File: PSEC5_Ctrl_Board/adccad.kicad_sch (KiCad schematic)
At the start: 0 parts

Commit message: Ports are Finished, wiring and finalization needed
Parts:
- added U13, U14: LTC2600CGN_PBF, LTC2600CGN_PBF:SSOP-16_GN, symbol PSEC5_ctrlbd:LTC2600CGN_PBF
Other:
- note added: "DAC"
- note added: "DAC 1"
- note added: "DAC 2"
- note added: "From FPGA"
- note added: "To Samtec"

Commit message: Large Updates, Touching up before further aproval
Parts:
- added C23: 0.1u, symbol Device:C
- added C35, C45, C80: 0.1u, Capacitor_SMD:C_0201_0603Metric, symbol Device:C_Small
- added R17: 7.5k, symbol Device:R_US
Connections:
- net GND: now reaches U14.1 (GND)
- net GND: now also U13.1 (GND), U13.10 (SDO), C23.2, C35.2, C45.2, C80.2
- net DAC2_VCC_5V0: now reaches U14.16 (VCC)
- net DAC2_VCC_5V0: now also U13.16 (VCC), C35.1, C45.1, R17.2
- net DISCBIAS: now reaches U14.2 (VOUTA)
- net WBUFBIAS: now reaches U14.3 (VOUTB)
- net READBIAS1: now reaches U14.4 (VOUTC)
- net READBIAS2: now reaches U14.5 (VOUTD)
- net DAC_VRef: now reaches U14.6 (REF)
- net DAC_VRef: now also U13.6 (REF), C23.1, C80.1
- net at U13.11 (*CLR): now also R17.1
- net THRES5: now reaches U13.12 (VOUTE)
- net THRES6: now reaches U13.13 (VOUTF)
- net THRES7: now reaches U13.14 (VOUTG)
- net THRES8: now reaches U13.15 (VOUTH)
- net THRES1: now reaches U13.2 (VOUTA)
- net THRES2: now reaches U13.3 (VOUTB)
- net THRES3: now reaches U13.4 (VOUTC)
- net THRES4: now reaches U13.5 (VOUTD)
- net DAC2_CS/LD: now reaches U13.7 (*CS/LD)
- net DAC2_SCK: now reaches U13.8 (SCK)
- net DAC2_SDI: now reaches U13.9 (SDI)
- no-connect marks 0 -> 4
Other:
- moved on the sheet: U13, U14

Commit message: minor changes
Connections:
- net THRES1 renamed Disc_Thresh1
- net THRES2 renamed Disc_Thresh2
- net THRES3 renamed Disc_Thresh3
- net THRES4 renamed Disc_Thresh4
- net THRES5 renamed Disc_Thresh5
- net THRES6 renamed Disc_Thresh6
- net THRES7 renamed Disc_Thresh7
- net THRES8 renamed Disc_Thresh8
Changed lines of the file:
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@@
 		)
 	)
-	(global_label "THRES1"
+	(global_label "Disc_Thresh1"
 		(shape output)
 		(at 74.93 54.61 0)
@@
 		)
 		(property "Intersheetrefs" "${INTERSHEET_REFS}"
-			(at 85.0513 54.61 0)
-			(effects
-				(font
-					(size 1.27 1.27)
-				)
-				(justify left)
-				(hide yes)
-			)
-		)
-	)
-	(global_label "THRES4"
+			(at 90.2523 54.61 0)
+			(effects
+				(font
+					(size 1.27 1.27)
+				)
+				(justify left)
+				(hide yes)
+			)
+		)
+	)
+	(global_label "Disc_Thresh4"
 		(shape output)
 		(at 74.93 62.23 0)
@@
 		)
 		(property "Intersheetrefs" "${INTERSHEET_REFS}"
-			(at 85.0513 62.23 0)
+			(at 90.2523 62.23 0)
 			(effects
 				(font
@@
 		)
 	)
-	(global_label "THRES8"
+	(global_label "Disc_Thresh8"
 		(shape output)
 		(at 74.93 72.39 0)
@@
 		)
 		(property "Intersheetrefs" "${INTERSHEET_REFS}"
-			(at 85.0513 72.39 0)
-			(effects
-				(font
-					(size 1.27 1.27)
-				)
-				(justify left)
-				(hide yes)
-			)
-		)
-	)
-	(global_label "THRES2"
+			(at 90.2523 72.39 0)
+			(effects
+				(font
+					(size 1.27 1.27)
+				)
+				(justify left)
+				(hide yes)
+			)
+		)
+	)
+	(global_label "Disc_Thresh2"
 		(shape output)
 		(at 74.93 57.15 0)
@@
 		)
 		(property "Intersheetrefs" "${INTERSHEET_REFS}"
-			(at 85.0513 57.15 0)
-			(effects
-				(font
-					(size 1.27 1.27)
-				)
-				(justify left)
-				(hide yes)
-			)
-		)
-	)
-	(global_label "THRES7"
+			(at 90.2523 57.15 0)
+			(effects
+				(font
+					(size 1.27 1.27)
+				)
+				(justify left)
+				(hide yes)
+			)
+		)
+	)
+	(global_label "Disc_Thresh7"
 		(shape output)
 		(at 74.93 69.85 0)
@@
 		)
 		(property "Intersheetrefs" "${INTERSHEET_REFS}"
-			(at 85.0513 69.85 0)
-			(effects
-				(font
-					(size 1.27 1.27)
-				)
-				(justify left)
-				(hide yes)
-			)
-		)
-	)
-	(global_label "THRES6"
+			(at 90.2523 69.85 0)
+			(effects
+				(font
+					(size 1.27 1.27)
+				)
+				(justify left)
+				(hide yes)
+			)
+		)
+	)
+	(global_label "Disc_Thresh6"
 		(shape output)
 		(at 74.93 67.31 0)
@@
 		)
 		(property "Intersheetrefs" "${INTERSHEET_REFS}"
-			(at 85.0513 67.31 0)
-			(effects
-				(font
-					(size 1.27 1.27)
-				)
-				(justify left)
-				(hide yes)
-			)
-		)
-	)
-	(global_label "THRES5"
+			(at 90.2523 67.31 0)
+			(effects
+				(font
+					(size 1.27 1.27)
+				)
+				(justify left)
+				(hide yes)
+			)
+		)
+	)
+	(global_label "Disc_Thresh5"
 		(shape output)
 		(at 74.93 64.77 0)
@@
 		)
 		(property "Intersheetrefs" "${INTERSHEET_REFS}"
-			(at 85.0513 64.77 0)
+			(at 90.2523 64.77 0)
 			(effects
 				(font
@@
 		)
 	)
-	(global_label "THRES3"
+	(global_label "Disc_Thresh3"
 		(shape output)
 		(at 74.93 59.69 0)
@@
 		)
 		(property "Intersheetrefs" "${INTERSHEET_REFS}"
-			(at 85.0513 59.69 0)
-			(effects
-				(font
+			(at 90.2523 59.69 0)
+			(effects
+				(font

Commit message: Schematic is "done" ;( (999+ ERC errors)
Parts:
- added R56: 7.5k, Capacitor_SMD:C_0603_1608Metric, symbol Device:R_US
- C90: renamed from C23; footprint (none) -> Capacitor_SMD:C_0603_1608Metric
- R77: renamed from R17; footprint (none) -> Capacitor_SMD:C_0603_1608Metric
- renumbered C35 to C92
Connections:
- net DAC2_CS/LD is gone; now on net CS/LD_DAC*: U13.7 (*CS/LD)
- net DAC2_SCK is gone; now on net SCK_DAC: U13.8 (SCK)
- net GND: now also U14.10 (SDO)
- net at U14.11 (*CLR): now also R56.1
- net CS/LD_DAC*: now reaches U14.7 (*CS/LD)
- net SCK_DAC: now reaches U14.8 (SCK)
- net SDI_DAC_BIAS: now reaches U14.9 (SDI)
- net DAC2_SDI renamed SDI_DAC_THRES
- net DAC2_VCC_5V0 renamed 3V3_DUT
- net 3V3_DUT: no longer R77.2
- net DAC_VRef renamed 1V8_DUT
- new net CLR_DAC*: R56.2, R77.2
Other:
- note added: "Currently, both DAC's have the following pins shorted:* *CS/LD* SCK *CLR However, the SDI pins are independent of eachother"
- note added: "From Kria"
- note added: "NOTE: DAC will run at 3V3"
- note added: "To DUT"
- note removed: "DAC"
- note removed: "DAC 1"
- note removed: "DAC 2"
- note removed: "From FPGA"
- note removed: "To Samtec"

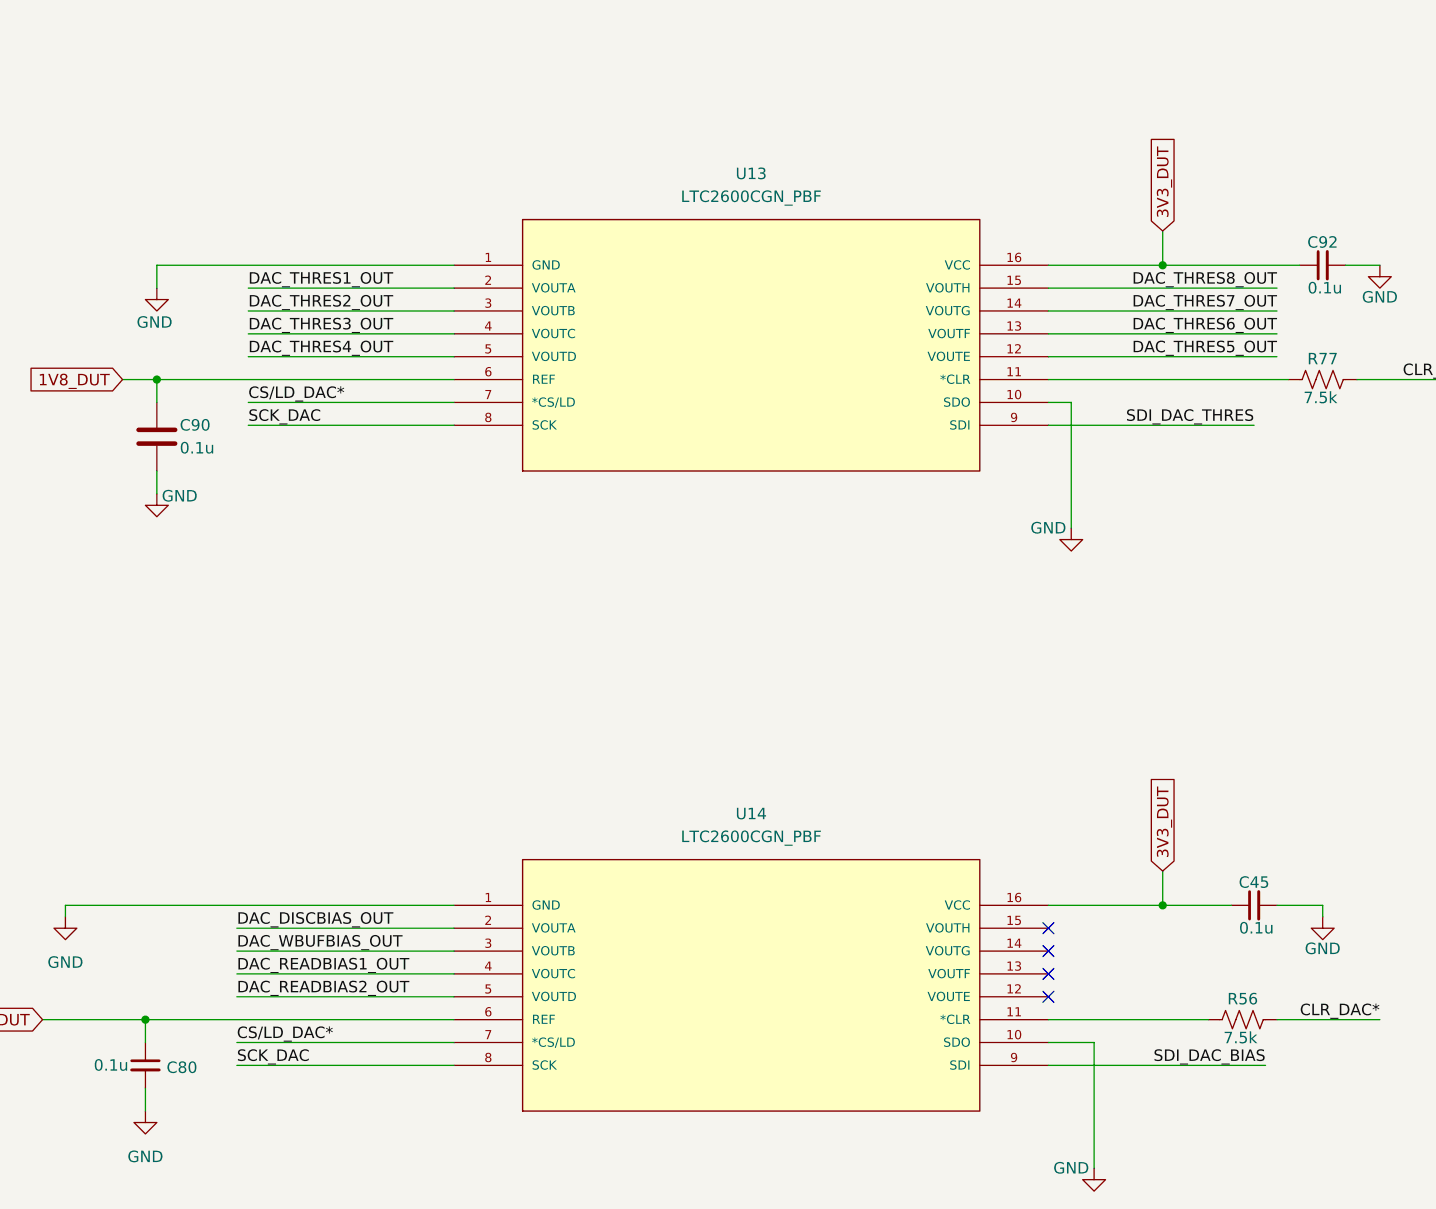
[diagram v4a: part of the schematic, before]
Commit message: Deleted some Pages, still lots of errors :(
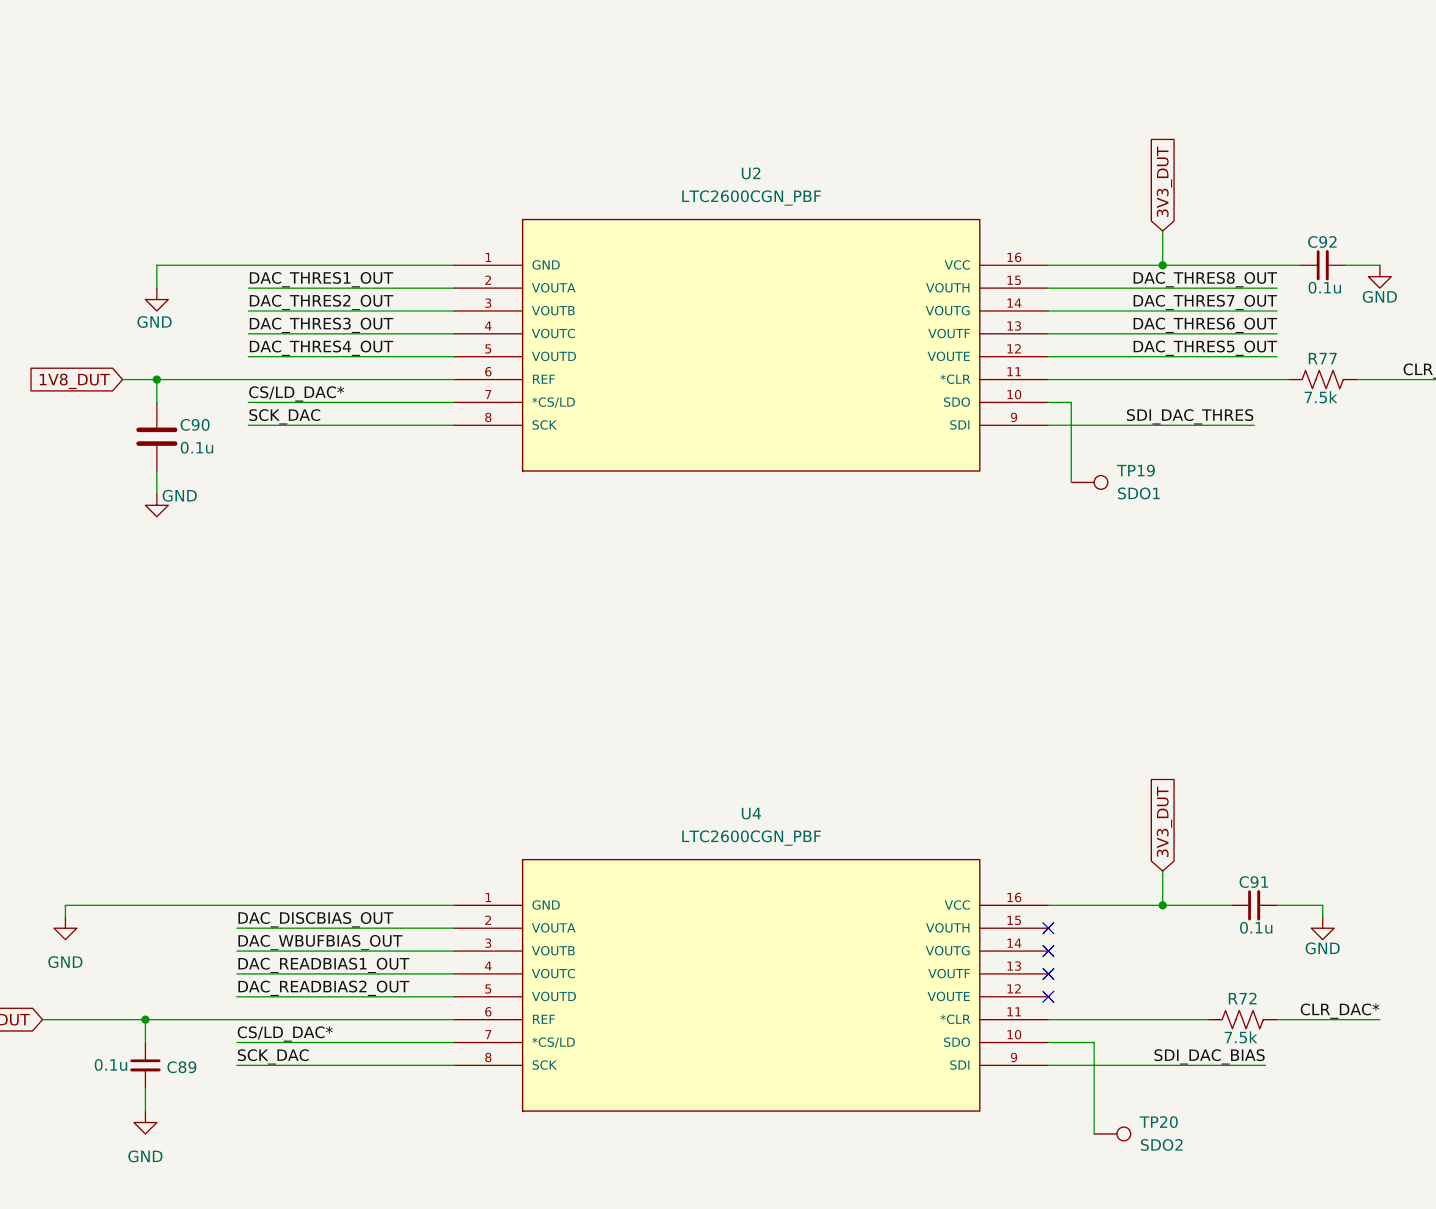
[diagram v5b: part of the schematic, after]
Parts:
- added TP19: SDO1, symbol Connector:TestPoint
- added TP20: SDO2, symbol Connector:TestPoint
- renumbered C80 to C89, C45 to C91, R56 to R72, U13 to U2, U14 to U4
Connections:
- net GND: no longer U2.10 (SDO), U4.10 (SDO)
- new net: TP19.1, U2.10 (SDO)
- new net: TP20.1, U4.10 (SDO)
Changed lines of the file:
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@@
-	(wire
-		(pts
-			(xy 218.44 91.44) (xy 218.44 77.47)
-		)
-		(stroke
-			(width 0)
-			(type default)
-		)
-	)
 	(wire
 		(pts
@@
 	(wire
 		(pts
-			(xy 220.98 148.59) (xy 220.98 162.56)
-		)
-		(stroke
-			(width 0)
-			(type default)
-		)
-	)
-	(wire
-		(pts
 			(xy 116.84 64.77) (xy 116.84 62.23)
 		)
@@
 	(wire
 		(pts
+			(xy 220.98 148.59) (xy 220.98 158.75)
+		)
+		(stroke
+			(width 0)
+			(type default)
+		)
+	)
+	(wire
+		(pts
 			(xy 218.44 77.47) (xy 215.9 77.47)
 		)
@@
 		(pts
 			(xy 250.19 74.93) (xy 264.16 74.93)
+		)
+		(stroke
+			(width 0)
+			(type default)
+		)
+	)
+	(wire
+		(pts
+			(xy 218.44 77.47) (xy 218.44 86.36)
 		)
 		(stroke
@@
 			)
 			(justify right)
+		)
+	)
+	(symbol
+		(lib_id "Connector:TestPoint")
+		(at 218.44 86.36 270)
+		(unit 1)
+		(exclude_from_sim no)
+		(in_bom yes)
+		(on_board yes)
+		(dnp no)
+		(fields_autoplaced yes)
+		(property "Reference" "TP19"
+			(at 223.52 85.0899 90)
+			(effects
+				(font
+					(size 1.27 1.27)
+				)
+				(justify left)
+			)
+		)
+		(property "Value" "SDO1"
+			(at 223.52 87.6299 90)
+			(effects
+				(font
+					(size 1.27 1.27)
+				)
+				(justify left)
+			)
+		)
+		(property "Footprint" ""
+			(at 218.44 91.44 0)
+			(effects
+				(font
+					(size 1.27 1.27)
+				)
+				(hide yes)
+			)
+		)
+		(property "Datasheet" "~"
+			(at 218.44 91.44 0)
+			(effects
+				(font
+					(size 1.27 1.27)
+				)
+				(hide yes)
+			)
+		)
+		(property "Description" "test point"
+			(at 218.44 86.36 0)
+			(effects
+				(font
+					(size 1.27 1.27)
+				)
+				(hide yes)
+			)
+		)
+		(pin "1"
+		)
+		(instances
+			(project ""
+				(path "/165f2ae6-d522-4adf-a6c4-bb137b209d33/1f6d7a03-cfad-4370-8d2b-49ab19e248d8/9bd9ffce-acff-4ff9-8380-cb9ceb30e6db"
+					(reference "TP19")
+					(unit 1)
+				)
+			)
 		)
 	)
@@
 		(on_board yes)
 		(dnp no)
-		(property "Reference" "#PWR053"
+		(property "Reference" "#PWR0113"
 			(at 116.84 93.98 0)
 			(effects
@@
 		(instances
 			(project "PSEC5_Ctrl_Board"
-				(path "/165f2ae6-d522-4adf-a6c4-bb137b209d33/7f8209d2-4c0c-4014-a327-54471b9e4269"
-					(reference "#PWR053")
-					(unit 1)
-				)
 				(path "/165f2ae6-d522-4adf-a6c4-bb137b209d33/1f6d7a03-cfad-4370-8d2b-49ab19e248d8/9bd9ffce-acff-4ff9-8380-cb9ceb30e6db"
 					(reference "#PWR0113")
@@
 	(symbol
 		(lib_id "power:GND")
-		(at 220.98 162.56 0)
-		(unit 1)
-		(exclude_from_sim no)
-		(in_bom yes)
-		(on_board yes)
-		(dnp no)
-		(property "Reference" "#PWR044"
-			(at 220.98 168.91 0)
-			(effects
-				(font
-					(size 1.27 1.27)
-				)
-				(hide yes)
-			)
-		)
-		(property "Value" "GND"
-			(at 218.44 162.56 0)
-			(effects
-				(font
-					(size 1.27 1.27)
-				)
-			)
-		)
-		(property "Footprint" ""
-			(at 220.98 162.56 0)
-			(effects
-				(font
-					(size 1.27 1.27)
-				)
-				(hide yes)
-			)
-		)
-		(property "Datasheet" ""
-			(at 220.98 162.56 0)
-			(effects
-				(font
-					(size 1.27 1.27)
-				)
-				(hide yes)
-			)
-		)
-		(property "Description" "Power symbol creates a global label with name \"GND\" , ground"
-			(at 220.98 162.56 0)
-			(effects
-				(font
-					(size 1.27 1.27)
-				)
-				(hide yes)
-			)
-		)
-		(pin "1"
-		)
-		(instances
-			(project "PSEC5_Ctrl_Board"
-				(path "/165f2ae6-d522-4adf-a6c4-bb137b209d33/7f8209d2-4c0c-4014-a327-54471b9e4269"
-					(reference "#PWR044")
-					(unit 1)
-				)
-				(path "/165f2ae6-d522-4adf-a6c4-bb137b209d33/1f6d7a03-cfad-4370-8d2b-49ab19e248d8/9bd9ffce-acff-4ff9-8380-cb9ceb30e6db"
-					(reference "#PWR0115")
-					(unit 1)
-				)
-			)
-		)
-	)
-	(symbol
-		(lib_id "power:GND")
 		(at 106.68 134.62 0)
 		(unit 1)
@@
 		(dnp no)
 		(fields_autoplaced yes)
-		(property "Reference" "U14"
+		(property "Reference" "U4"
 			(at 182.88 123.19 0)
 			(effects
@@
 		)
 		(pin "5"
-		)
-		(instances
-			(project "PSEC5_Ctrl_Board"
-				(path "/165f2ae6-d522-4adf-a6c4-bb137b209d33/7f8209d2-4c0c-4014-a327-54471b9e4269"
-					(reference "U14")
-					(unit 1)
-				)
-				(path "/165f2ae6-d522-4adf-a6c4-bb137b209d33/1f6d7a03-cfad-4370-8d2b-49ab19e248d8/9bd9ffce-acff-4ff9-8380-cb9ceb30e6db"
-					(reference "U4")
-					(unit 1)
-				)
-			)
-		)
-	)
-	(symbol
-		(lib_id "power:GND")
-		(at 218.44 91.44 0)
-		(unit 1)
-		(exclude_from_sim no)
-		(in_bom yes)
-		(on_board yes)
-		(dnp no)
-		(property "Reference" "#PWR0114"
-			(at 218.44 97.79 0)
-			(effects
-				(font
-					(size 1.27 1.27)
-				)
-				(hide yes)
-			)
-		)
-		(property "Value" "GND"
-			(at 215.9 91.44 0)
-			(effects
-				(font
-					(size 1.27 1.27)
-				)
-			)
-		)
-		(property "Footprint" ""
-			(at 218.44 91.44 0)
-			(effects
-				(font
-					(size 1.27 1.27)
-				)
-				(hide yes)
-			)
-		)
-		(property "Datasheet" ""
-			(at 218.44 91.44 0)
-			(effects
-				(font
-					(size 1.27 1.27)
-				)
-				(hide yes)
-			)
-		)
-		(property "Description" "Power symbol creates a global label with name \"GND\" , ground"
-			(at 218.44 91.44 0)
-			(effects
-				(font
-					(size 1.27 1.27)
-				)
-				(hide yes)
-			)
-		)
-		(pin "1"
 		)
 		(instances
 			(project "PSEC5_Ctrl_Board"
 				(path "/165f2ae6-d522-4adf-a6c4-bb137b209d33/1f6d7a03-cfad-4370-8d2b-49ab19e248d8/9bd9ffce-acff-4ff9-8380-cb9ceb30e6db"
-					(reference "#PWR0114")
+					(reference "U4")
 					(unit 1)
 				)
@@
 		(on_board yes)
 		(dnp no)
-		(property "Reference" "C45"
+		(property "Reference" "C91"
 			(at 238.76 130.81 90)
 			(effects
@@
 		(instances
 			(project "PSEC5_Ctrl_Board"
-				(path "/165f2ae6-d522-4adf-a6c4-bb137b209d33/7f8209d2-4c0c-4014-a327-54471b9e4269"
-					(reference "C45")
-					(unit 1)
-				)
 				(path "/165f2ae6-d522-4adf-a6c4-bb137b209d33/1f6d7a03-cfad-4370-8d2b-49ab19e248d8/9bd9ffce-acff-4ff9-8380-cb9ceb30e6db"
 					(reference "C91")
@@
 		(dnp no)
 		(fields_autoplaced yes)
-		(property "Reference" "U13"
+		(property "Reference" "U2"
 			(at 182.88 52.07 0)
 			(effects
@@
 		(instances
 			(project "PSEC5_Ctrl_Board"
-				(path "/165f2ae6-d522-4adf-a6c4-bb137b209d33/7f8209d2-4c0c-4014-a327-54471b9e4269"
-					(reference "U13")
-					(unit 1)
-				)
 				(path "/165f2ae6-d522-4adf-a6c4-bb137b209d33/1f6d7a03-cfad-4370-8d2b-49ab19e248d8/9bd9ffce-acff-4ff9-8380-cb9ceb30e6db"
 					(reference "U2")
@@
 	)
 	(symbol
+		(lib_id "Connector:TestPoint")
+		(at 220.98 158.75 270)
+		(unit 1)
+		(exclude_from_sim no)
+		(in_bom yes)
+		(on_board yes)
+		(dnp no)
+		(fields_autoplaced yes)
+		(property "Reference" "TP20"
+			(at 226.06 157.4799 90)
+			(effects
+				(font
+					(size 1.27 1.27)
+				)
+				(justify left)
+			)
+		)
+		(property "Value" "SDO2"
+			(at 226.06 160.0199 90)
+			(effects
+				(font
+					(size 1.27 1.27)
+				)
+				(justify left)
+			)
+		)
+		(property "Footprint" ""
+			(at 220.98 163.83 0)
+			(effects
+				(font
+					(size 1.27 1.27)
+				)
+				(hide yes)
+			)
+		)
+		(property "Datasheet" "~"
+			(at 220.98 163.83 0)
+			(effects
+				(font
+					(size 1.27 1.27)
+				)
+				(hide yes)
+			)
+		)
+		(property "Description" "test point"
+			(at 220.98 158.75 0)
+			(effects
+				(font
+					(size 1.27 1.27)
+				)
+				(hide yes)
+			)
+		)
+		(pin "1"
+		)
+		(instances
+			(project "PSEC5_Ctrl_Board"
+				(path "/165f2ae6-d522-4adf-a6c4-bb137b209d33/1f6d7a03-cfad-4370-8d2b-49ab19e248d8/9bd9ffce-acff-4ff9-8380-cb9ceb30e6db"
+					(reference "TP20")
+					(unit 1)
+				)
+			)
+		)
+	)
+	(symbol
 		(lib_id "Device:C_Small")
 		(at 115.57 151.13 0)
@@
 		(on_board yes)
 		(dnp no)
-		(property "Reference" "C80"
+		(property "Reference" "C89"
 			(at 119.634 151.384 0)
 			(effects
@@
 		(instances
 			(project "PSEC5_Ctrl_Board"
-				(path "/165f2ae6-d522-4adf-a6c4-bb137b209d33/7f8209d2-4c0c-4014-a327-54471b9e4269"
-					(reference "C80")
-					(unit 1)
-				)
 				(path "/165f2ae6-d522-4adf-a6c4-bb137b209d33/1f6d7a03-cfad-4370-8d2b-49ab19e248d8/9bd9ffce-acff-4ff9-8380-cb9ceb30e6db"
 					(reference "C89")
@@
 		(on_board yes)
 		(dnp no)
-		(property "Reference" "R56"
+		(property "Reference" "R72"
 			(at 237.49 143.764 90)
 			(effects
@@
 		(instances
 			(project "PSEC5_Ctrl_Board"
-				(path "/165f2ae6-d522-4adf-a6c4-bb137b209d33/7f8209d2-4c0c-4014-a327-54471b9e4269"
-					(reference "R56")
-					(unit 1)
-				)
 				(path "/165f2ae6-d522-4adf-a6c4-bb137b209d33/1f6d7a03-cfad-4370-8d2b-49ab19e248d8/9bd9ffce-acff-4ff9-8380-cb9ceb30e6db"
 					(reference "R72")
